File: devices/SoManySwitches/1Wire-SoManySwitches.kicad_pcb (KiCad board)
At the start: 2 copper layers, 192.9 x 41.3 mm, 24 parts, among them J1 RJ45, J10 RJ45, J2 RJ45, J3 RJ45, J4 RJ45, J5 RJ45, J6 RJ45, J7 RJ45, J8 RJ45, J9 RJ45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

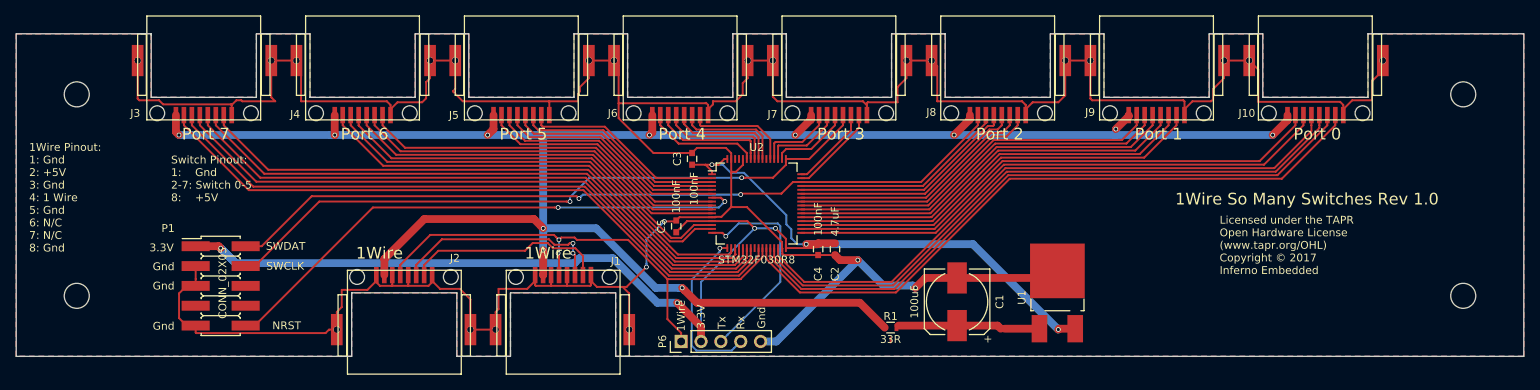
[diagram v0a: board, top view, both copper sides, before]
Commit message: Bump all active boards to Revision 1.2
- Remove dropping resistor from 5V power line
- Add pullup resistor to Reset line
- Add pin markings to STM32 chip footprint

Signed-off-by: Alastair D'Silva <alastair@d-silva.org>
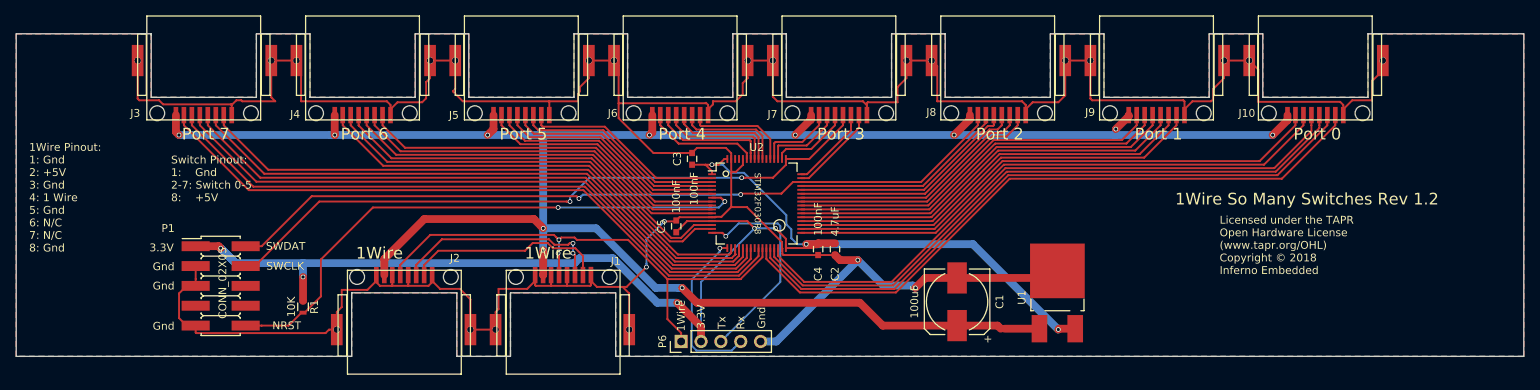
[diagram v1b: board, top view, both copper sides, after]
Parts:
- removed REF1, REF2, REF3, REF4: MountingHole_3.2mm_M3, Mounting_Holes:MountingHole_3.2mm_M3
- R1: value 33R -> 10K
- moved R1 75.2 mm to (73.4, 94.5), turned to 270 degrees
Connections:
- C1 pad 1: Net-(C1-Pad1) -> +5V
- J7 pad 8: +5V -> Net-(J7-Pad8)
- J8 pad 8: +5V -> Net-(J7-Pad8)
- P1 pad 6: (no net) -> Net-(P1-Pad6)
- P1 pad 7: (no net) -> Net-(P1-Pad7)
- P1 pad 8: (no net) -> Net-(P1-Pad8)
- R1 pad 1: +5V -> +3V3
- R1 pad 2: Net-(C1-Pad1) -> Net-(P1-Pad10)
- U1 pad 1: Net-(C1-Pad1) -> +5V
- U2 pad 24: (no net) -> Net-(U2-Pad24)
- U2 pad 61: (no net) -> Net-(U2-Pad61)
- U2 pad 62: (no net) -> Net-(U2-Pad62)
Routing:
- net +5V: track 256.6 -> 276.4 mm
- net Net-(C1-Pad1): track 18.6 -> 0.00 mm
- net +3V3: track 179.2 -> 184.1 mm, vias 7 -> 8
- net Net-(P1-Pad10): track 69.7 -> 73.7 mm
- net (no net): track 0.64 -> 0.00 mm
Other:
- board text added: "1Wire So Many Switches Rev 1.2"
- board text added: "Licensed under the TAPR Open Hardware License (www.tapr.org/OHL) Copyright © 2018 Inferno Embedded"
- board text removed: "1Wire So Many Switches Rev 1.0"
- board text removed: "Licensed under the TAPR Open Hardware License (www.tapr.org/OHL) Copyright © 2017 Inferno Embedded"
